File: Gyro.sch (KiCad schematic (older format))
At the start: 4 parts, among them U7 MPU-6000

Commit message: Lots of changes made
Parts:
- removed C45: 0.1uF, Capacitor_SMD:C_0402_1005Metric, symbol Device:C_Small
- removed C46: 2.2nF, Capacitor_SMD:C_0402_1005Metric, symbol Device:C_Small
- removed U7: MPU-6000, Sensor_Motion:InvenSense_QFN-24_4x4mm_P0.5mm, symbol Sensor_Motion:MPU-6000
- added C19, C20, C21, C22: 0.1uF, Capacitor_SMD:C_0402_1005Metric, symbol Device:C_Small
- added U5: SN74AXC4T774RSVR, Footprints:SN74AXC4T774RSVR, symbol JPW_Symbols:SN74AXC4T774RSVR
- added U6: ICM-20948, Sensor_Motion:InvenSense_QFN-24_3x3mm_P0.4mm, symbol Sensor_Motion:ICM-20948
- renumbered C47 to C18
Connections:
- net GND: now also C19.2, C20.2, C21.2, C22.2, U5.6 (DIR4), U5.7 (OE_N), U5.8 (GND), U6.18 (GND), U6.20 (GND)
- net SPI1_CS: now also U5.1 (A1)
- net SPI1_MISO: now also U5.4 (A4)
- net SPI1_MOSI: now also U5.3 (A3)
- net SPI1_SCK: now also U5.2 (A2)
- net +3V3: now reaches C18.1
- net +3V3: now also U5.14 (VCCA), U5.15 (DIR1), U5.16 (DIR2), U5.5 (DIR3)
- new net +1V8: C19.1, C20.1, C21.1, U5.13 (VCCB), U6.13 (VDD), U6.8 (VDDIO)
- new net ICM_CS: U5.12 (B1), U6.22 (~CS)
- new net ICM_MISO: U5.9 (B4), U6.9 (SDO/AD0)
- new net ICM_MOSI: U5.10 (B3), U6.24 (SDA/SDI)
- new net ICM_SCK: U5.11 (B2), U6.23 (SCL/SCLK)
- new net REGOUT: C22.1, U6.10 (REGOUT)
- no-connect marks 3 -> 4
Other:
- moved on the sheet: C18

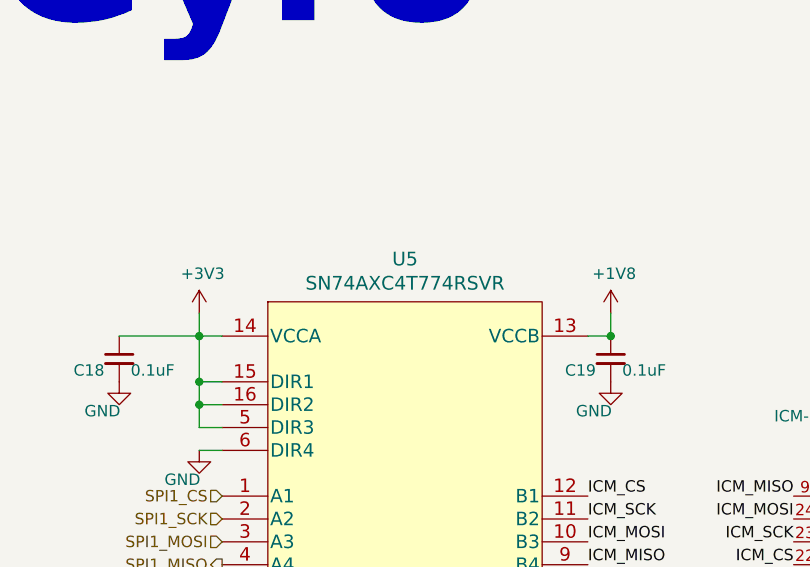
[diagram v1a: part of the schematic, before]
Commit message: Cosmetic changes to schematic
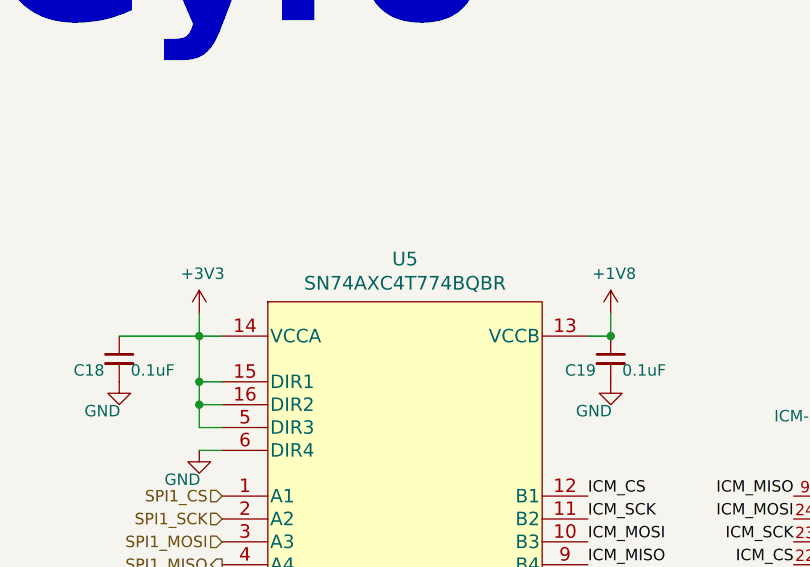
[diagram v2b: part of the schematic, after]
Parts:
- removed U5: SN74AXC4T774RSVR, Footprints:SN74AXC4T774RSVR, symbol JPW_Symbols:SN74AXC4T774RSVR
- added U5: SN74AXC4T774BQBR, Footprints:SN74AXC4T774BQBR, symbol JPW_Symbols:SN74AXC4T774BQBR
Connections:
- net +1V8: now also U5.13 (VCCB)
- net +3V3: now also U5.14 (VCCA), U5.15 (DIR1), U5.16 (DIR2), U5.5 (DIR3)
- net GND: now also U5.6 (DIR4), U5.7 (OE_N), U5.8 (GND)
- net ICM_CS: now also U5.12 (B1)
- net ICM_MISO: now also U5.9 (B4)
- net ICM_MOSI: now also U5.10 (B3)
- net ICM_SCK: now also U5.11 (B2)
- net SPI1_CS: now also U5.1 (A1)
- net SPI1_MISO: now also U5.4 (A4)
- net SPI1_MOSI: now also U5.3 (A3)
- net SPI1_SCK: now also U5.2 (A2)
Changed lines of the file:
@@
 $EndComp
 $Comp
-L JPW_Symbols:SN74AXC4T774RSVR U5
-U 1 1 6182BAA4
-P 6750 3650
-F 0 "U5" H 6750 4587 60  0000 C CNN
-F 1 "SN74AXC4T774RSVR" H 6750 4481 60  0000 C CNN
-F 2 "Footprints:SN74AXC4T774RSVR" H 6750 3590 60  0001 C CNN
-F 3 "" H 6750 3650 60  0000 C CNN
-	1    6750 3650
-	1    0    0    -1
-$EndComp
-$Comp
 L power:+3V3 #PWR029
 U 1 1 6182F8E8
@@
 $EndBitmap
 Connection ~ 7650 3050
+$Comp
+L JPW_Symbols:SN74AXC4T774BQBR U5
+U 1 1 618236BF
+P 6750 3650
+F 0 "U5" H 6750 4587 60  0000 C CNN
+F 1 "SN74AXC4T774BQBR" H 6750 4481 60  0000 C CNN
+F 2 "Footprints:SN74AXC4T774BQBR" H 6750 3590 60  0001 C CNN
+F 3 "" H 6750 3650 60  0000 C CNN
+	1    6750 3650
+	1    0    0    -1
+$EndComp
 $EndSCHEMATC

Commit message: Changes made
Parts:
- removed C20, C21, C22: 0.1uF, Capacitor_SMD:C_0402_1005Metric, symbol Device:C_Small
- removed U5: SN74AXC4T774BQBR, Footprints:SN74AXC4T774BQBR, symbol JPW_Symbols:SN74AXC4T774BQBR
- removed U6: ICM-20948, Sensor_Motion:InvenSense_QFN-24_3x3mm_P0.4mm, symbol Sensor_Motion:ICM-20948
- added C18: 0.1uF, Capacitor_SMD:C_0402_1005Metric, symbol Device:C_Small
- added U5: MPU-6000, Sensor_Motion:InvenSense_QFN-24_4x4mm_P0.5mm, symbol Sensor_Motion:MPU-6000
- C19: value 0.1uF -> 2.2nF
- renumbered C18 to C20
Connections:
- net +3V3 is gone; now on net REGOUT: C20.1
- net GND: now also C18.2, U5.1 (CLKIN), U5.11 (FSYNC), U5.18 (GND)
- net REGOUT: now also U5.10 (REGOUT)
- net SPI1_CS: now also U5.8 (~CS)
- net SPI1_MISO: now also U5.9 (AD0/MISO)
- net SPI1_MOSI: now also U5.24 (SDA/MOSI)
- net SPI1_SCK: now also U5.23 (SCL/SCLK)
- net +1V8 renamed CPOUT
- net CPOUT: now also U5.20 (CPOUT)
- new net +3V3_GYRO: C18.1, U5.13 (VDD)
- no-connect marks 4 -> 3
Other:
- moved on the sheet: C20
